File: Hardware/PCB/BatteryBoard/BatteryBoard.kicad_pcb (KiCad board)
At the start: 2 copper layers, 60 x 60 mm, 78 parts, among them J1 USB_C_Receptacle_USB2.0, J2 Thermistor, J3 Conn_01x07, J4 Conn_01x07, J5 Conn_01x07, J6 Conn_01x07, J7 Power, Q1 FDS4935A, Q2 FDS4935A, SW1 SW_SPDT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

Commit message: バッテリモジュール完成
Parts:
- removed the J1 at (150.0, 66.2)
- added D3: ESDA13P70-1U1M, Diode_SMD_extlib:ESDA13P70-1U1M, F.Cu at (135.3, 113.1)
- added G***: LOGO, LOGO:Logo_BatteryBoard, F.Cu at (146.2, 83.5)
- C23: footprint Capacitor_SMD:C_1206_3216Metric -> Capacitor_SMD:C_0805_2012Metric
- J7: footprint Connector_AMASS:AMASS_XT30UPB-F_1x02_P5.0mm_Vertical -> Connector_PinHeader_2.54mm:PinHeader_1x04_P2.54mm_Vertical
- moved J7 20.7 mm to (122.1, 105.1), turned to 180 degrees
- moved C23 0.64 mm to (125.8, 125.3)
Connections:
- J7 pad 1: GND -> +5V
- J7 pad 2: +5V -> GND
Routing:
- net +3.3V: track 0.00 -> 32.0 mm
- net Net-(BT1-Pad2): track 10.8 -> 27.1 mm
- net +5V: track 0.00 -> 14.8 mm
- net Net-(R24-Pad1): track 0.00 -> 4.41 mm
- net Net-(R25-Pad1): track 0.00 -> 4.41 mm
- net Net-(R28-Pad1): track 0.00 -> 2.93 mm
- net Net-(R26-Pad1): track 0.00 -> 2.93 mm
- net Net-(C21-Pad1): track 0.00 -> 2.17 mm
- net Net-(C20-Pad1): track 0.00 -> 2.17 mm
- net Net-(SW1-Pad2): track 19.4 -> 18.5 mm
- net GND: vias 6 -> 235
- added copper zone on In1.Cu, net +3.3V
- added copper zone on In2.Cu, net +5V
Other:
- copper layers 2 -> 4
- board text added: "3V3"
- board text added: "5V"
- board text added: "GND"
- board text added: "INT"
- board text added: "NC"
- board text added: "PSEL"
- board text added: "SCL"
- board text added: "SDA"

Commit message: バッテリモジュールの部品表を生成
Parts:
- C1, C10, C7: value 10u(3225) -> 10μF100V X7S 3225
- C16, C17: value 10u(3225) -> 47μF16V X6S 3225
- C18, C19: value 0.1u -> 1u
- C22: value 10u(3216) -> 100μF10V X5R 3216
- C23: value 10u(3216) -> 10μF35V X5R 2012
- C24: value 22u(3216) -> 100μF10V X5R 3216
- C25: value 22u(3216) -> 220μF4V X6S 3216
- C30, C31: value 4.7u -> 4.7μF50V X7S 2012
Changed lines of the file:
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@@
       (effects (font (size 1 1) (thickness 0.15)))
     )
-    (fp_text value "10u(3216)" (at 0 1.68 -90) (layer "F.Fab")
+    (fp_text value "10μF35V X5R 2012" (at 0 1.68 -90) (layer "F.Fab")
       (effects (font (size 1 1) (thickness 0.15)))
     )
@@
       (effects (font (size 1 1) (thickness 0.15)))
     )
-    (fp_text value "0.1u" (at 0 1.43 90) (layer "F.Fab")
+    (fp_text value "1u" (at 0 1.43 90) (layer "F.Fab")
       (effects (font (size 1 1) (thickness 0.15)))
     )
@@
       (effects (font (size 1 1) (thickness 0.15)))
     )
-    (fp_text value "4.7u" (at 0 1.68 90) (layer "F.Fab")
+    (fp_text value "4.7μF50V X7S 2012" (at 0 1.68 90) (layer "F.Fab")
       (effects (font (size 1 1) (thickness 0.15)))
     )
@@
       (effects (font (size 1 1) (thickness 0.15)))
     )
-    (fp_text value "10u(3225)" (at 0 2.3) (layer "F.Fab")
+    (fp_text value "47μF16V X6S 3225" (at 0 2.3) (layer "F.Fab")
       (effects (font (size 1 1) (thickness 0.15)))
     )
@@
       (effects (font (size 1 1) (thickness 0.15)))
     )
-    (fp_text value "10u(3225)" (at 0 2.3 135) (layer "F.Fab")
+    (fp_text value "10μF100V X7S 3225" (at 0 2.3 135) (layer "F.Fab")
       (effects (font (size 1 1) (thickness 0.15)))
     )
@@
       (effects (font (size 1 1) (thickness 0.15)))
     )
-    (fp_text value "10u(3216)" (at 0 1.85 90) (layer "F.Fab")
+    (fp_text value "100μF10V X5R 3216" (at 0 1.85 90) (layer "F.Fab")
       (effects (font (size 1 1) (thickness 0.15)))
     )
@@
       (effects (font (size 1 1) (thickness 0.15)))
     )
-    (fp_text value "22u(3216)" (at 0 1.85 90) (layer "F.Fab")
+    (fp_text value "220μF4V X6S 3216" (at 0 1.85 90) (layer "F.Fab")
       (effects (font (size 1 1) (thickness 0.15)))
     )
@@
       (effects (font (size 1 1) (thickness 0.15)))
     )
-    (fp_text value "0.1u" (at 0 1.43 90) (layer "F.Fab")
+    (fp_text value "1u" (at 0 1.43 90) (layer "F.Fab")
       (effects (font (size 1 1) (thickness 0.15)))
     )
@@
       (effects (font (size 1 1) (thickness 0.15)))
     )
-    (fp_text value "10u(3225)" (at 0 2.3) (layer "F.Fab")
+    (fp_text value "10μF100V X7S 3225" (at 0 2.3) (layer "F.Fab")
       (effects (font (size 1 1) (thickness 0.15)))
     )
@@
       (effects (font (size 1 1) (thickness 0.15)))
     )
-    (fp_text value "10u(3225)" (at 0 2.3) (layer "F.Fab")
+    (fp_text value "47μF16V X6S 3225" (at 0 2.3) (layer "F.Fab")
       (effects (font (size 1 1) (thickness 0.15)))
     )
@@
       (effects (font (size 1 1) (thickness 0.15)))
     )
-    (fp_text value "22u(3216)" (at 0 1.85 90) (layer "F.Fab")
+    (fp_text value "100μF10V X5R 3216" (at 0 1.85 90) (layer "F.Fab")
       (effects (font (size 1 1) (thickness 0.15)))
     )
@@
       (effects (font (size 1 1) (thickness 0.15)))
     )
-    (fp_text value "4.7u" (at 0 1.68 90) (layer "F.Fab")
+    (fp_text value "4.7μF50V X7S 2012" (at 0 1.68 90) (layer "F.Fab")
       (effects (font (size 1 1) (thickness 0.15)))
     )
@@
       (effects (font (size 1 1) (thickness 0.15)))
     )
-    (fp_text value "10u(3225)" (at 0 2.3 45) (layer "F.Fab")
+    (fp_text value "10μF100V X7S 3225" (at 0 2.3 45) (layer "F.Fab")
       (effects (font (size 1 1) (thickness 0.15)))
     )

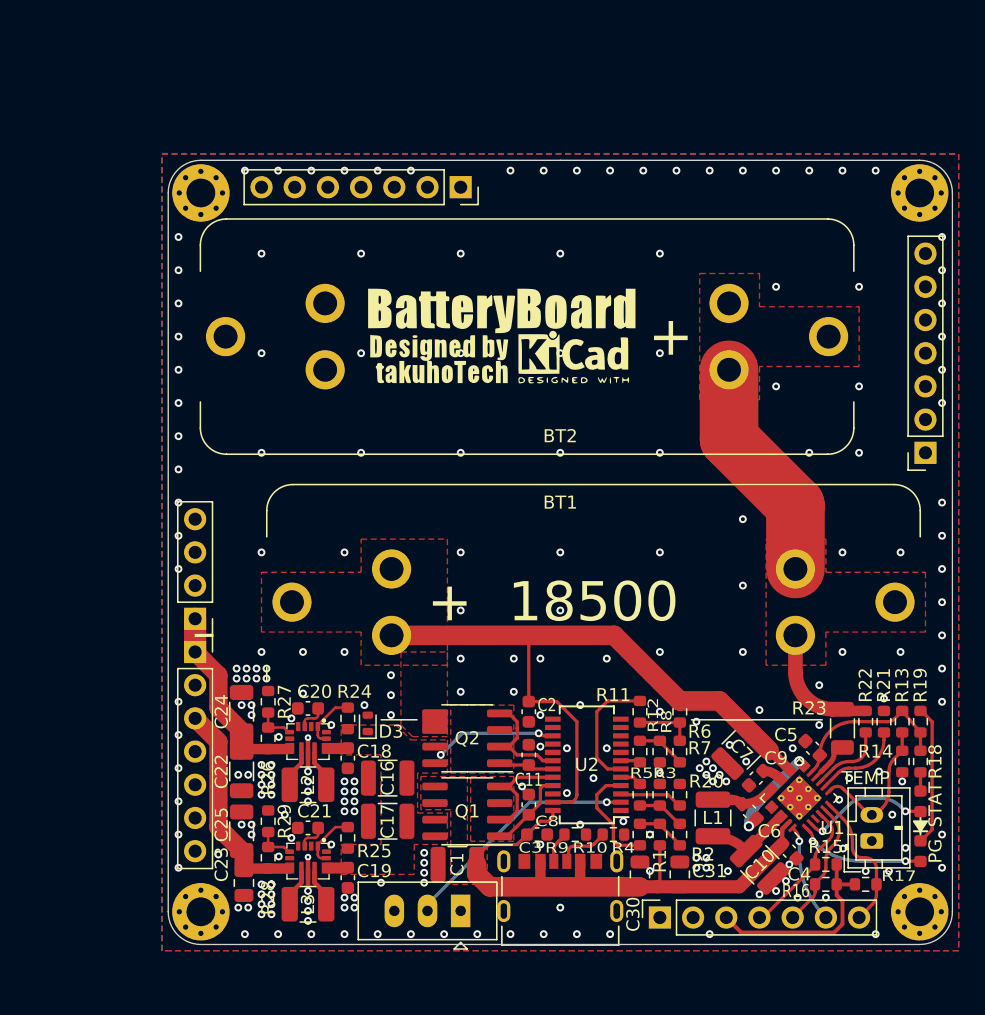
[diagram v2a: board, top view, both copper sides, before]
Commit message: ヒューズを追加、バッテリクリップの下のベタをBATTネットに
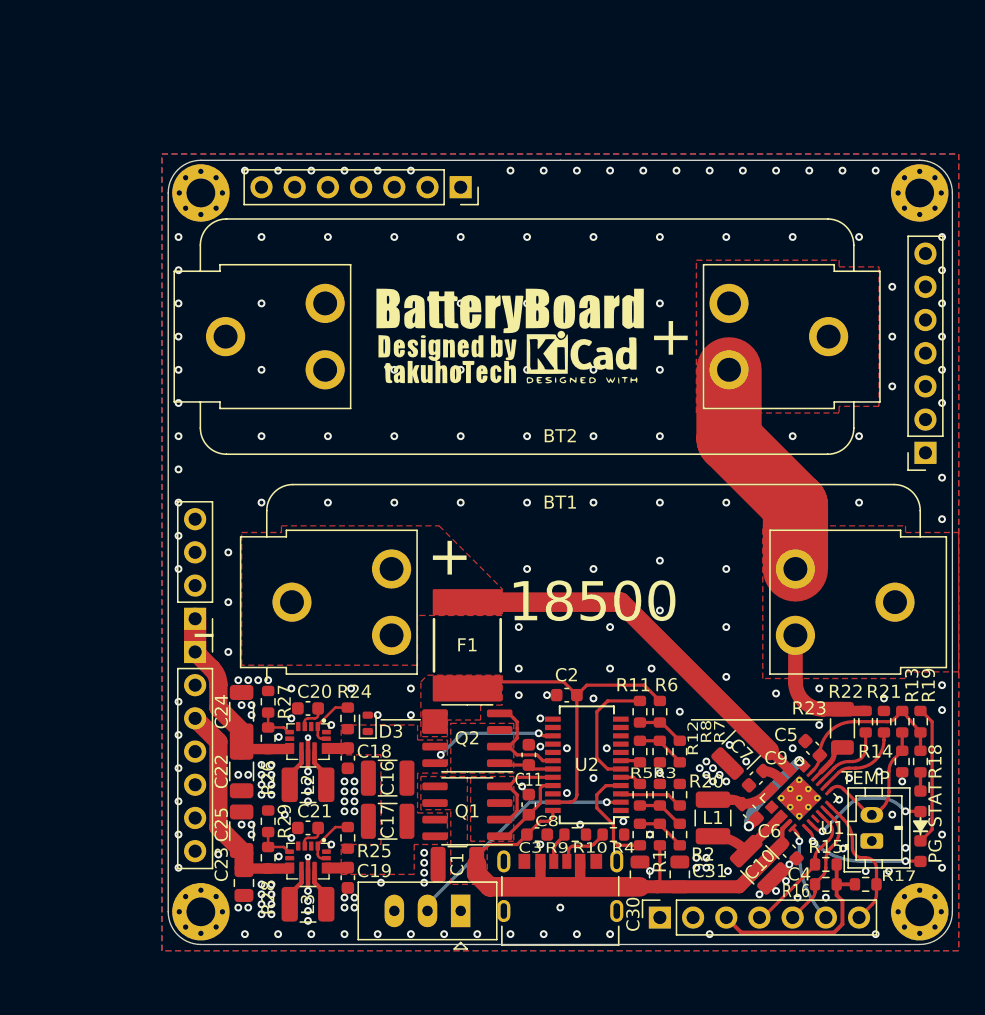
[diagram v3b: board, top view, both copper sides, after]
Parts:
- added F1: ASMDC300F/24-2, ASMDC300F_24-2:ASMDC300F_24-2, F.Cu at (142.9, 107.1)
- moved C2 3.17 mm to (150.5, 110.9), turned to 180 degrees
- moved R6 1.52 mm to (157.6, 112.2)
- moved G*** 0.63 mm to (146.8, 83.5)
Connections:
- C2 pad 1: +BATT -> VBAT
- Q2 pad 5: +BATT -> VBAT
- Q2 pad 6: +BATT -> VBAT
- R6 pad 1: +BATT -> VBAT
- U2 pad 23: +BATT -> VBAT
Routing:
- net VBAT: track 0.00 -> 25.9 mm
- net +BATT: track 51.9 -> 30.0 mm
- net Net-(R11-Pad2): track 4.45 -> 3.63 mm
- net GND: vias 235 -> 241
- added copper zone on F.Cu, net VBAT
